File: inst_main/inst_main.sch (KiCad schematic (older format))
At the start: 7 parts, among them J1 B2B-XH-A(LF)(SN), J2 B2B-XH-A(LF)(SN), J3 B2B-XH-A(LF)(SN), P1 ANALOG, P2 DIGITAL_L, P3 DIGITAL_H

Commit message: mod inst_main rev0.1
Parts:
- added C?: 0.1u, symbol C
- added P?: CONN_02X18, symbol CONN_02X18
- added R? (x3): 2k, symbol R
- added R? (x3): 3k, symbol R
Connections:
- net 3V3: now also P?.4 (P4), C?.1
- net 5V: now also P?.1 (P1), P?.2 (P2)
- net GND: now also P?.6 (P6), C?.2, P?.35 (P35), P?.36 (P36), R?.1, R?.1, R?.1
- net DAT2: now reaches P?.1 (P1)
- net SWA: now reaches P?.10 (P10)
- net CD/DAT3: now reaches P?.2 (P2)
- net CD/DAT3: now also R?.2, R?.2
- net CMD: now reaches P?.3 (P3)
- net CMD: now also R?.2, R?.2
- net CLK: now reaches P?.5 (P5)
- net CLK: now also R?.2, R?.2
- net D51/MOSI: now reaches P?.7 (P7)
- net D51/MOSI: now also P?.32 (P32)
- net DAT1: now reaches P?.8 (P8)
- net SWB: now reaches P?.9 (P9)
- new net D22: P?.3 (P3)
- new net D23: P?.4 (P4)
- new net D24: P?.5 (P5)
- new net D25: P?.6 (P6)
- new net D26: P?.7 (P7)
- new net D27: P?.8 (P8)
- new net D28: P?.9 (P9)
- new net D29: P?.10 (P10)
- new net D30: P?.11 (P11)
- new net D31: P?.12 (P12)
- new net D32: P?.13 (P13)
- new net D33: P?.14 (P14)
- new net D34: P?.15 (P15)
- new net D35: P?.16 (P16)
- new net D36: P?.17 (P17)
- new net D37: P?.18 (P18)
- new net D38: P?.19 (P19)
- new net D39: P?.20 (P20)
- new net D40: P?.21 (P21)
- new net D41: P?.22 (P22)
- new net D42: P?.23 (P23)
- new net D43: P?.24 (P24)
- new net D44: P?.25 (P25)
- new net D45: P?.26 (P26)
- new net D46: P?.27 (P27)
- new net D47: P?.28 (P28)
- new net D48: P?.29 (P29)
- new net D49: P?.30 (P30)
- new net D50/MISO: P?.31 (P31), R?.1
- new net D52/SCK: P?.33 (P33), R?.1
- new net D53/SS: P?.34 (P34), R?.1
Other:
- note added: "0.1"
- note added: "2017/06/02"
- note added: "inst."
- note removed: "2.2"
- note removed: "2017/05/02"
- note removed: "Servo ctrl."
- moved on the sheet: P1, P2, P3

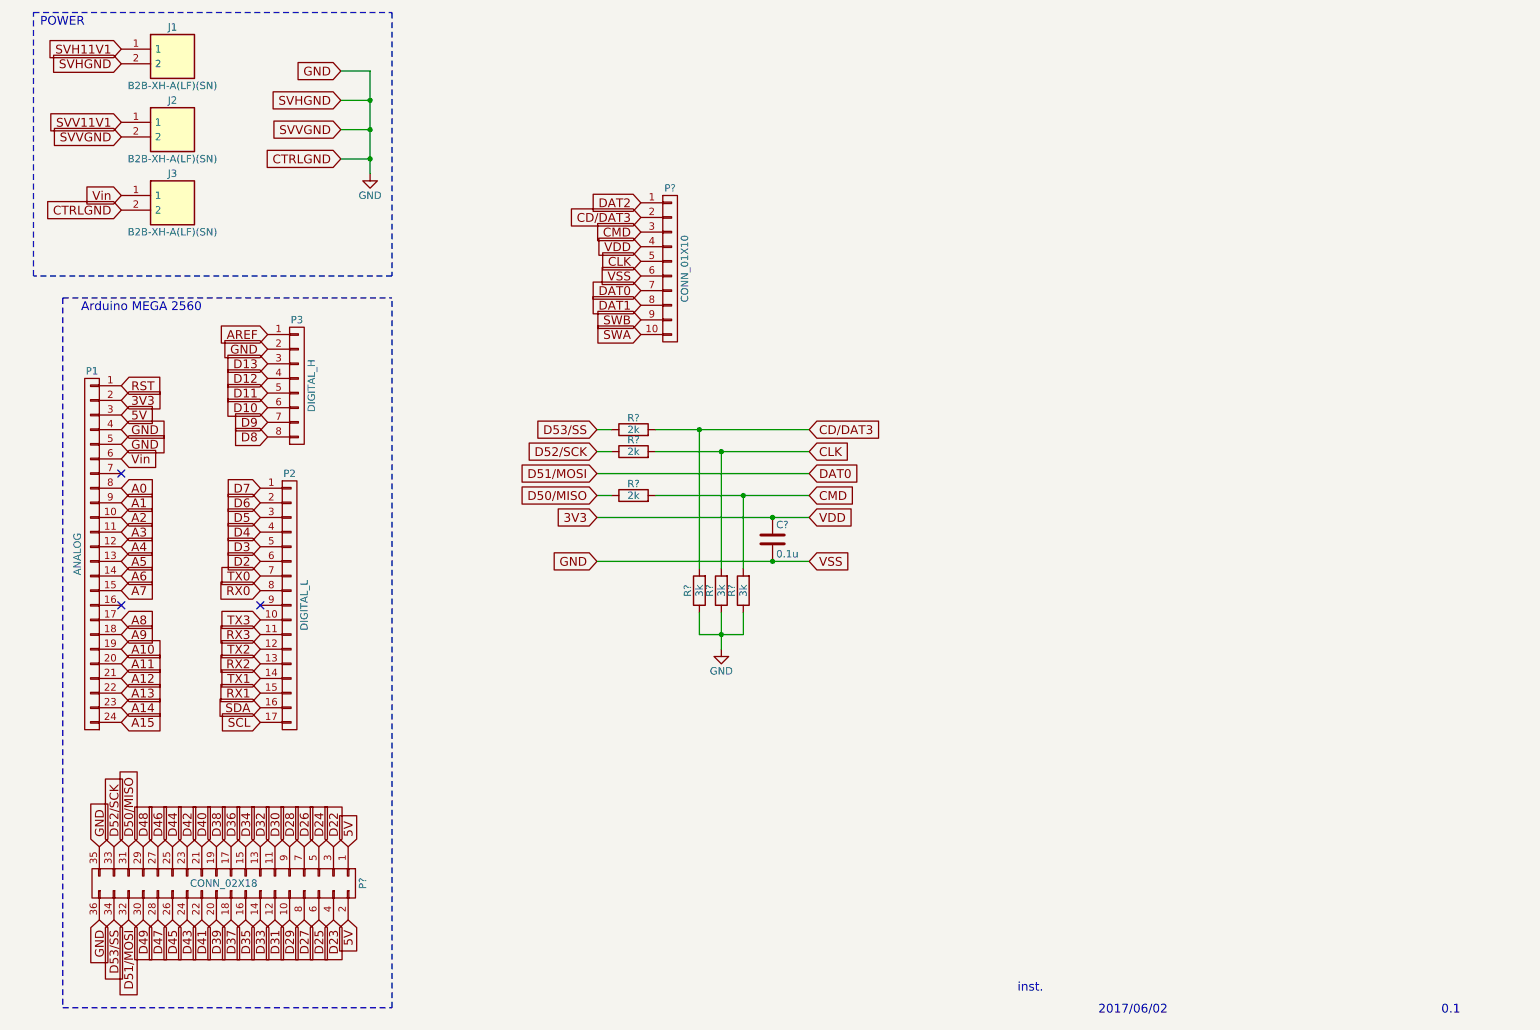
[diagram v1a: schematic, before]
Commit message: mod inst_main sch and pcb (Rev. 0.2)
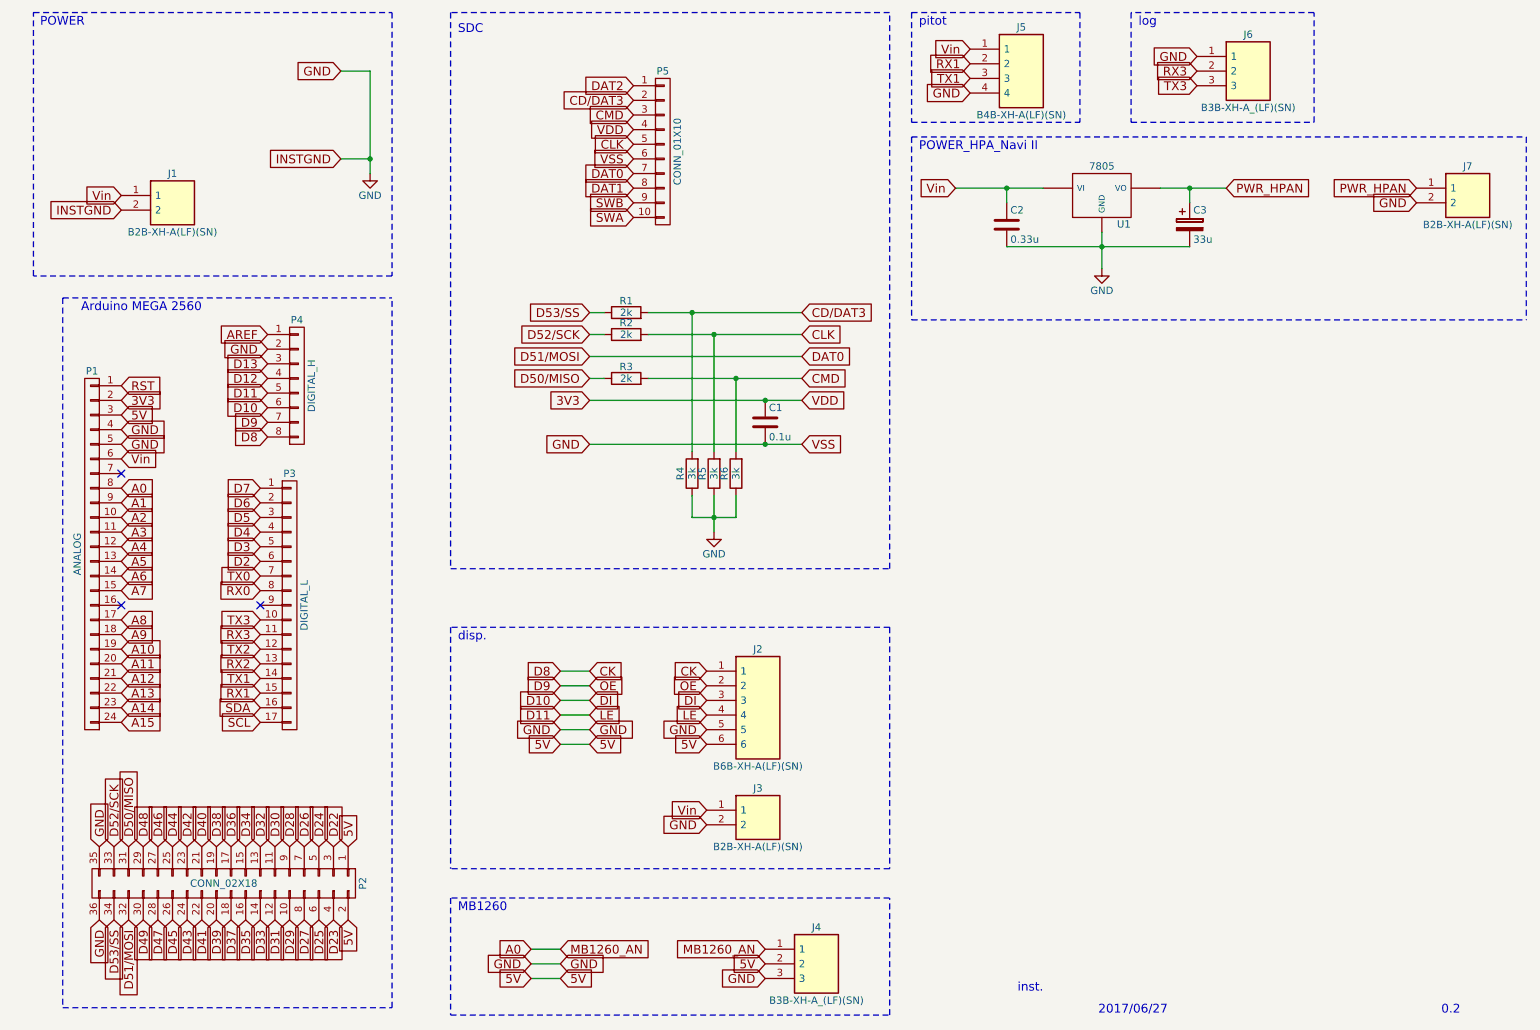
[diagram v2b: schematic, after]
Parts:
- removed J1, J2: B2B-XH-A(LF)(SN), Pin_Headers:Pin_Header_Straight_1x02_Pitch2.54mm, symbol B2B-XH-A(LF)(SN)
- added C2: 0.33u, Capacitors_ThroughHole:C_Disc_D3.0mm_W1.6mm_P2.50mm, symbol C
- added C3: 33u, Capacitors_ThroughHole:CP_Radial_D6.3mm_P2.50mm, symbol CP
- added J2: B6B-XH-A(LF)(SN), Pin_Headers:Pin_Header_Straight_1x06_Pitch2.54mm, symbol B6B-XH-A(LF)(SN)
- added J3, J7: B2B-XH-A(LF)(SN), Pin_Headers:Pin_Header_Straight_1x02_Pitch2.54mm, symbol B2B-XH-A(LF)(SN)
- added J4, J6: B3B-XH-A_(LF)(SN), Pin_Headers:Pin_Header_Straight_1x03_Pitch2.54mm, symbol B3B-XH-A_(LF)(SN)
- added J5: B4B-XH-A(LF)(SN), Pin_Headers:Pin_Header_Straight_1x04_Pitch2.54mm, symbol B4B-XH-A(LF)(SN)
- added U1: 7805, TO_SOT_Packages_THT:TO-220_Vertical, symbol 7805
- C1: renamed from C?; footprint (none) -> Capacitors_ThroughHole:C_Disc_D3.0mm_W1.6mm_P2.50mm
- P2: renamed from P?; footprint (none) -> Pin_Headers:Pin_Header_Straight_2x18_Pitch2.54mm
- P5: renamed from P?; footprint (none) -> Pin_Headers:Pin_Header_Straight_1x10_Pitch2.54mm
- R1, R2, R3, R4, R5, R6: renamed from R?; footprint (none) -> Resistors_ThroughHole:R_Axial_DIN0204_L3.6mm_D1.6mm_P2.54mm_Vertical
- renumbered J3 to J1, P2 to P3, P3 to P4
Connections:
- net 5V: now also J2.6, J4.2
- net A0: now also J4.1
- net D10: now also J2.3
- net D11: now also J2.4
- net D9: now also J2.2
- net GND: now also C2.2, C3.2, J2.5, J3.2, J4.3, J5.4, J6.1, J7.2, U1.GND
- net RX1: now also J5.2
- net RX3: now also J6.2
- net TX1: now also J5.3
- net TX3: now also J6.3
- net Vin: now also C2.1, J3.1, J5.1, U1.VI
- net D8 renamed CK
- net CK: now also J2.1
- new net PWR_HPAN: C3.1, J7.1, U1.VO
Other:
- note added: "0.2"
- note added: "2017/06/27"
- note added: "MB1260"
- note added: "POWER_HPA_Navi II"
- note added: "SDC"
- note added: "disp."
- note added: "log"
- note added: "pitot"
- note removed: "0.1"
- note removed: "2017/06/02"
- moved on the sheet: C1, P5, R1, R2, R3, R4, R5, R6
